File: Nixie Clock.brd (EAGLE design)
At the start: 194.6 x 100.3 mm, 149 parts, among them IC1_SECONDS_UNITS 4017N, IC2_SECONDS_TENS 4017N, IC3_MINUTES_UNITS 4017N, IC4_MINUTES_TENS 4017N, IC5_HOURS_UNITS 4017N, IC6_HOURS_TENS 4017N, IC7_AND 4081N, T0 MPSA42, T1 MPSA42, T10 MPSA42, T11 MPSA42, T12 MPSA42, T13 MPSA42, T14 MPSA42, T15 MPSA42, T16 MPSA42, T17 MPSA42, T18 MPSA42, T19 MPSA42, T2 MPSA42, T20 MPSA42, T21 MPSA42, T22 MPSA42, T23 MPSA42, T24 MPSA42, T25 MPSA42, T26 MPSA42, T27 MPSA42, T28 MPSA42, T29 MPSA42, T3 MPSA42, T30 MPSA42, T31 MPSA42, T32 MPSA42, T33 MPSA42, T34 MPSA42, T35 MPSA42, T36 MPSA42, T37 MPSA42, T38 MPSA42, T39 MPSA42, T4 MPSA42, T40 MPSA42, T41 MPSA42, T42 MPSA42, T43 MPSA42, T44 MPSA42, T5 MPSA42, T6 MPSA42, T7 MPSA42, T8 MPSA42, T9 MPSA42

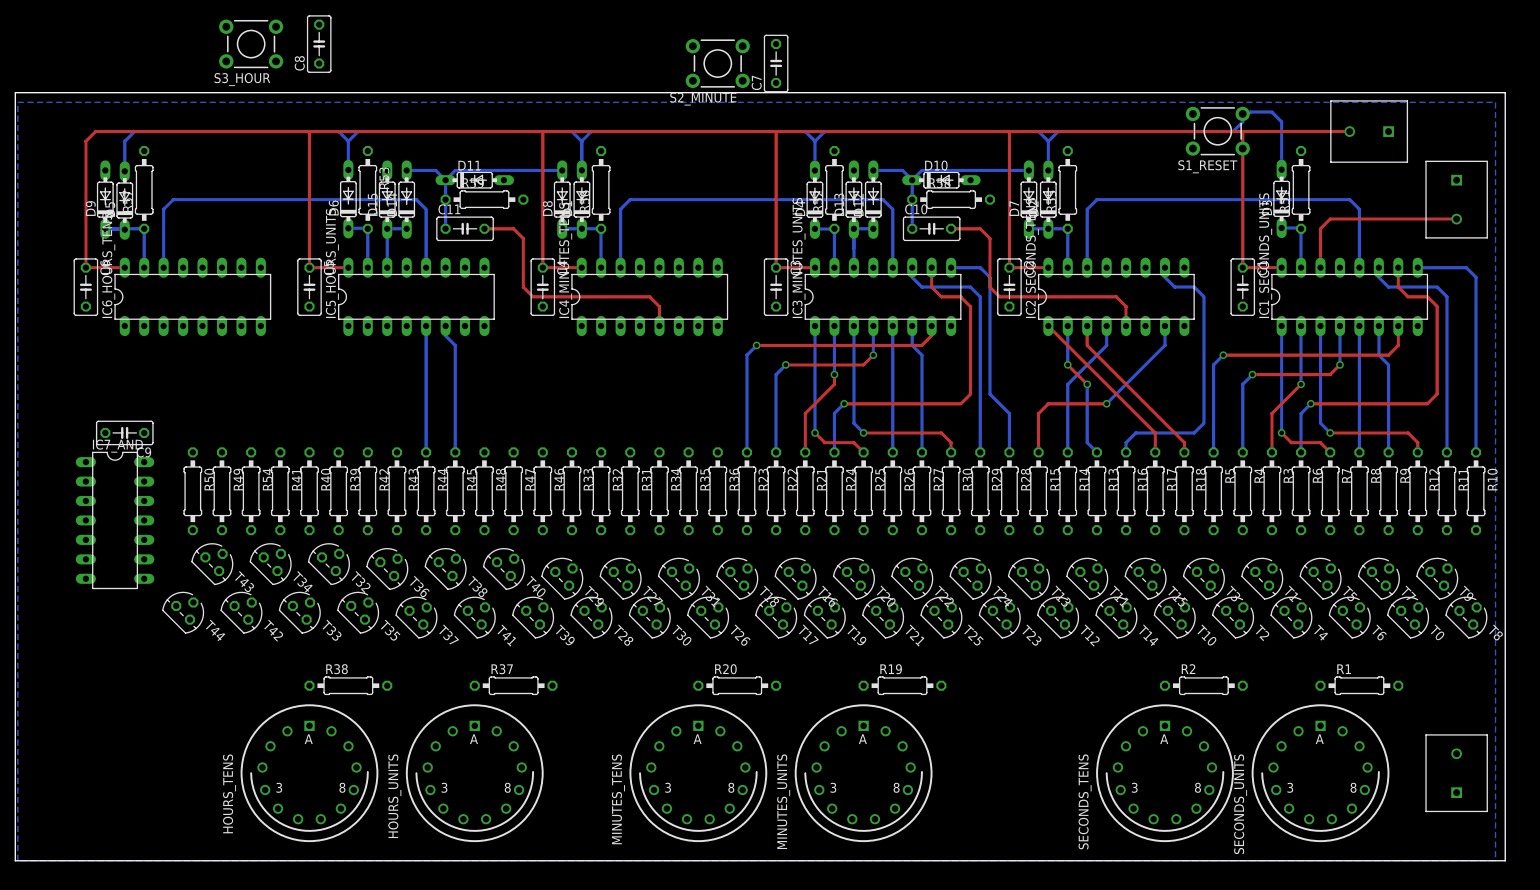
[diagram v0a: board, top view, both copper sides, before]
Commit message: Complete layout of control signals for 4017s
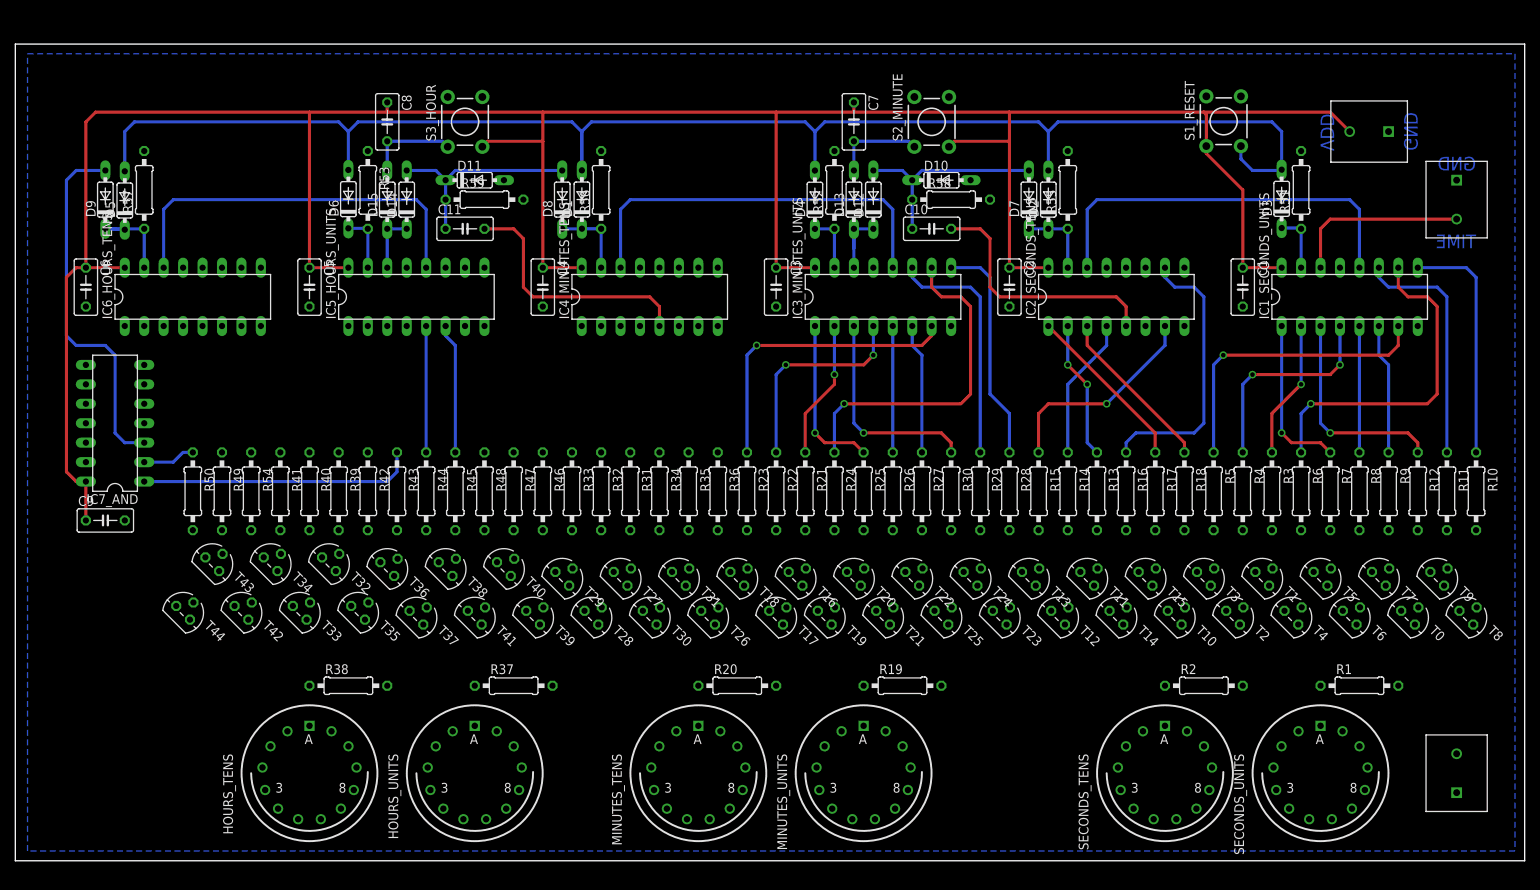
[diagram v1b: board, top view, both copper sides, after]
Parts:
- moved S3_HOUR 29.7 mm to (58.4, 96.5), turned to 90 degrees
- moved S2_MINUTE 29.0 mm to (119.4, 96.5), turned to 90 degrees
- moved C8 13.5 mm to (48.3, 96.5), turned to 270 degrees
- moved C7 12.7 mm to (109.2, 96.5), turned to 270 degrees
- moved IC7_AND 12.7 mm to (12.7, 57.1), turned to 90 degrees
- moved C9 11.7 mm to (11.4, 44.5), turned to 0 degrees
- moved S1_RESET 1.52 mm to (157.5, 96.6), turned to 90 degrees
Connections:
- net ADD_HOUR: now also S3_HOUR.1; no longer S3_HOUR.3
- net ADD_MINUTE: now also S2_MINUTE.1; no longer S2_MINUTE.3
- net VCC: now also S2_MINUTE.3, S3_HOUR.3; no longer S2_MINUTE.1, S3_HOUR.1
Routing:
- net VCC: track 301.5 -> 375.5 mm
- net RESET_HOURS: track 0.00 -> 47.8 mm
- net HOURS_5: track 0.00 -> 36.1 mm
- net MASTER_RESET: track 187.1 -> 199.6 mm
- net ADD_MINUTE: track 0.00 -> 12.0 mm
- net ADD_HOUR: track 0.00 -> 12.0 mm
- net THOURS_2: track 0.00 -> 6.88 mm
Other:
- board size 194.6 x 100.3 mm -> 197.2 x 106.7 mm
- board text added: "GND"
- board text added: "TIME"
- board text added: "VDD"

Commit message: Complete layout for 4017's outputs
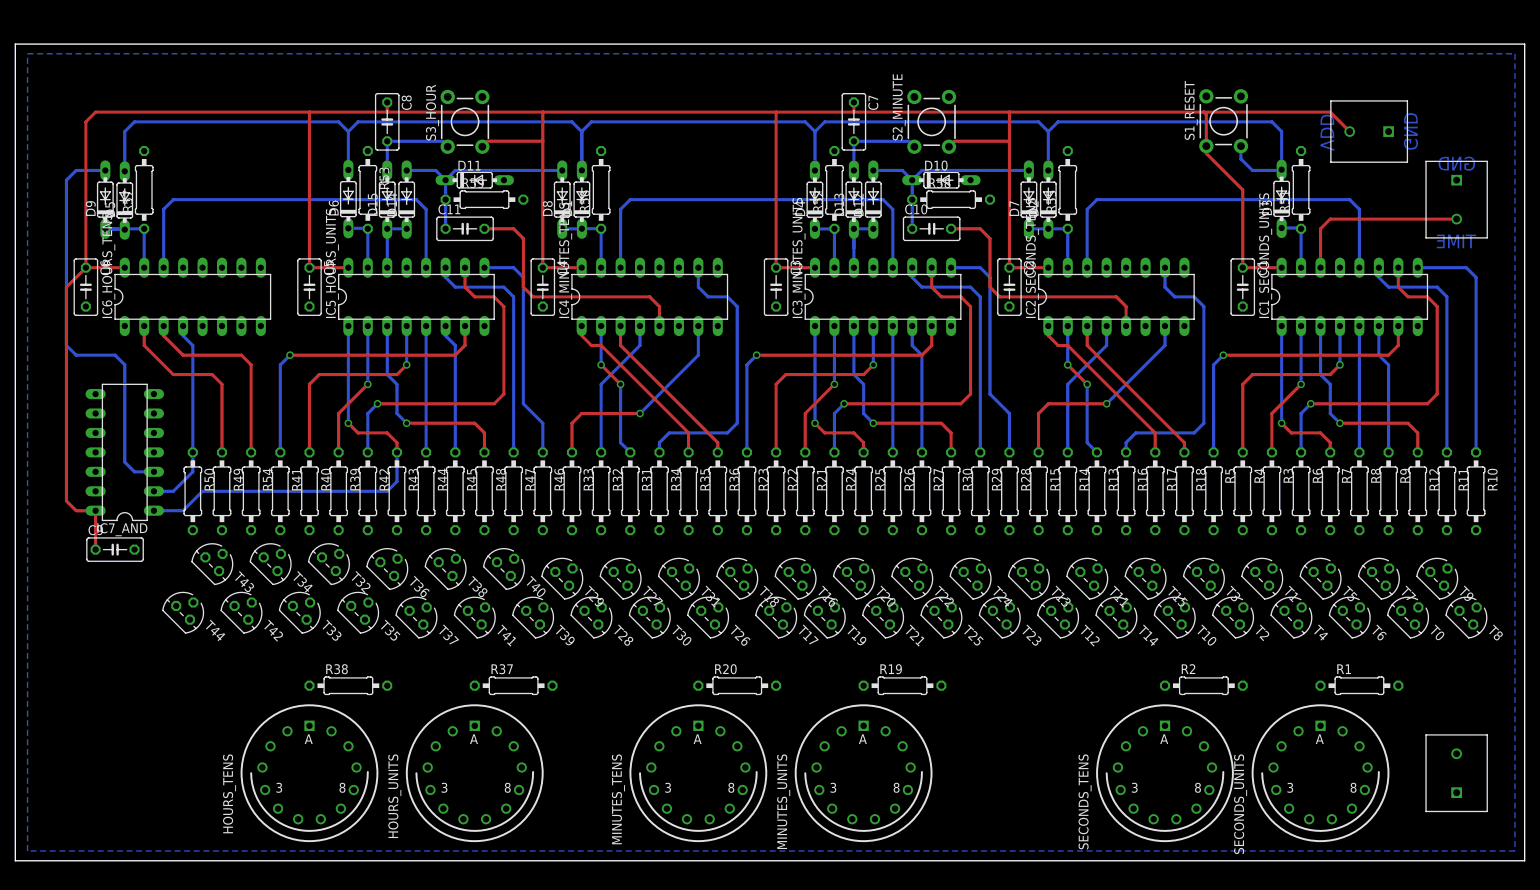
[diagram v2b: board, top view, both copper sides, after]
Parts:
- moved C9 4.02 mm to (12.7, 40.6)
- moved IC7_AND 4.02 mm to (14.0, 53.3)
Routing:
- net HOURS_4: track 0.00 -> 44.0 mm, vias 0 -> 1
- net HOURS_3: track 0.00 -> 39.2 mm, vias 0 -> 1
- net TMIN_4: track 0.00 -> 36.4 mm
- net HOURS_9: track 0.00 -> 31.5 mm
- net HOURS_8: track 0.00 -> 29.5 mm
- net TMIN_3: track 0.00 -> 27.8 mm, vias 0 -> 1
- net HOURS_2: track 0.00 -> 27.7 mm, vias 0 -> 1
- net HOURS_0: track 0.00 -> 27.0 mm, vias 0 -> 1
- net THOURS_0: track 0.00 -> 25.7 mm
- net THOURS_1: track 0.00 -> 23.7 mm
- net HOURS_5: track 36.1 -> 58.5 mm, vias 0 -> 1
- net TMIN_5: track 0.00 -> 21.8 mm
- net TMIN_0: track 0.00 -> 21.8 mm
- net THOURS_2: track 6.88 -> 25.7 mm
- net TMIN_2: track 0.00 -> 18.6 mm
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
